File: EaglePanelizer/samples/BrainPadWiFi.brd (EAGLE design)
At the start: 25.4 x 26 mm, 14 parts, among them IC1 ESP-WROOM-02FRONT-FACE, U2 TLV1117LV33DCYRDCY4-M

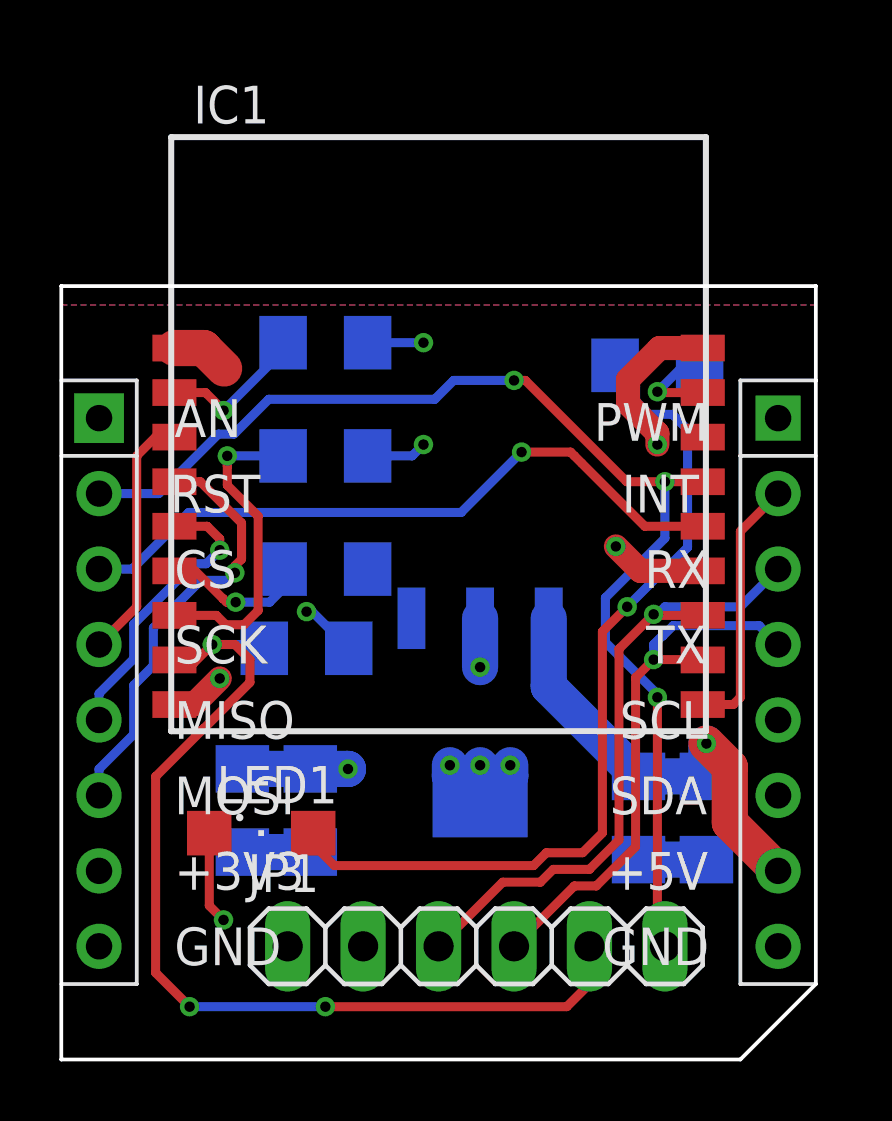
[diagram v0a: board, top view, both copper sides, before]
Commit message: Supported bugs for rendering gerber with duplicate same lines at the package dimension layer.
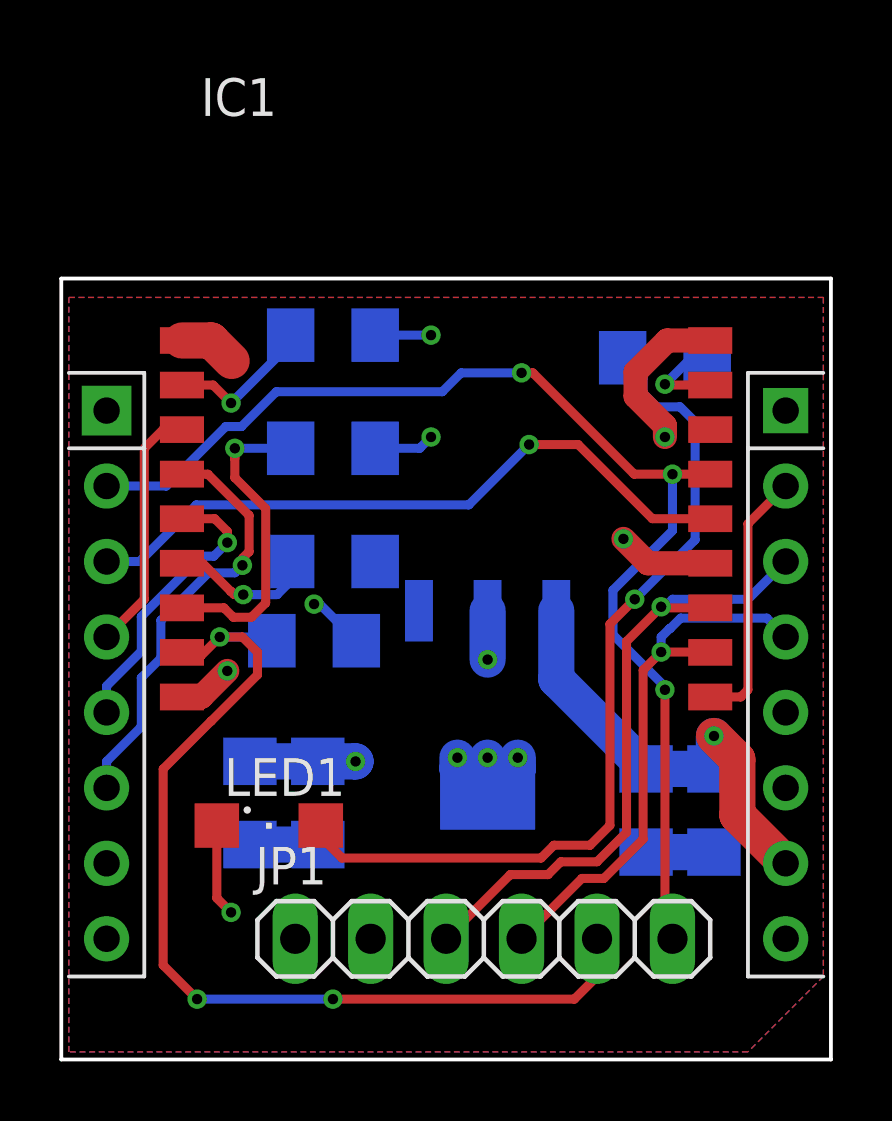
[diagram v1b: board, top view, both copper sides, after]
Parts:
- moved R4 0.36 mm to (20.3, 23.6)
- moved U2 0.36 mm to (14.4, 11.9)
- moved C4 0.36 mm to (22.0, 8.38)
- moved R1 0.36 mm to (9.14, 24.4)
- moved R2 0.36 mm to (9.14, 20.6)
- moved LED1 0.36 mm to (6.99, 7.87)
- moved U$1 0.36 mm to (0.25, 0.25)
- moved JP1 0.36 mm to (14.2, 4.06)
- moved C2 0.36 mm to (6.35, 8.64)
- moved C3 0.36 mm to (8.64, 8.64)
- moved IC1 0.36 mm to (13.0, 19.3)
- moved R3 0.36 mm to (8.51, 14.1)
- moved C1 0.36 mm to (19.7, 8.38)
- moved R5 0.36 mm to (9.14, 16.8)
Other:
- board size 25.4 x 26 mm -> 25.9 x 26.3 mm
